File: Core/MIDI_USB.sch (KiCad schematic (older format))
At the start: 25 parts, among them J1 Conn_01x04, J4 Conn_01x06, SW1 SW_Push_DPDT, U1 ATSAMD21G15B-A, U10 TLE9250V, U9 MCP2517FD-xSL, Y1 20MHz

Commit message: Update MIDI_USB.sch
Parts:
- C35: value 22nF -> 4.7nF
- R4, R5: value 120 -> 56
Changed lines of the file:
@@
 P 10700 3850
 F 0 "C35" H 10815 3896 50  0000 L CNN
-F 1 "22nF" H 10815 3805 50  0000 L CNN
+F 1 "4.7nF" H 10815 3805 50  0000 L CNN
 F 2 "Capacitor_SMD:C_0603_1608Metric" H 10738 3700 50  0001 C CNN
 F 3 "~" H 10700 3850 50  0001 C CNN
@@
 P 10450 3200
 F 0 "R4" V 10243 3200 50  0000 C CNN
-F 1 "120" V 10334 3200 50  0000 C CNN
+F 1 "56" V 10334 3200 50  0000 C CNN
 F 2 "Resistor_SMD:R_0603_1608Metric" V 10380 3200 50  0001 C CNN
 F 3 "~" H 10450 3200 50  0001 C CNN
@@
 P 10450 3600
 F 0 "R5" V 10243 3600 50  0000 C CNN
-F 1 "120" V 10334 3600 50  0000 C CNN
+F 1 "56" V 10334 3600 50  0000 C CNN
 F 2 "Resistor_SMD:R_0603_1608Metric" V 10380 3600 50  0001 C CNN
 F 3 "~" H 10450 3600 50  0001 C CNN

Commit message: Add custom footprints
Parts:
- J1: footprint CustomLib:MicroMatch_04_Angled -> Custom_FP:MicroMatch_04_Angled
- SW1: footprint CustomLib:SlideDPDT_JS202011 -> Custom_FP:SlideDPDT_JS202011
- Y1: footprint CustomLib:Crystal_2pin_2.0x2.5mm -> Custom_FP:Crystal_2pin_2.0x2.5mm
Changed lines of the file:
@@
 F 0 "SW1" H 10000 3985 50  0000 C CNN
 F 1 "SW_Push_DPDT" H 10000 3894 50  0000 C CNN
-F 2 "CustomLib:SlideDPDT_JS202011" H 10000 3700 50  0001 C CNN
+F 2 "Custom_FP:SlideDPDT_JS202011" H 10000 3700 50  0001 C CNN
 F 3 "~" H 10000 3700 50  0001 C CNN
 	1    10000 3500
@@
 F 0 "J1" H 10680 5092 50  0000 L CNN
 F 1 "Conn_01x04" H 10680 5001 50  0000 L CNN
-F 2 "CustomLib:MicroMatch_04_Angled" H 10600 5100 50  0001 C CNN
+F 2 "Custom_FP:MicroMatch_04_Angled" H 10600 5100 50  0001 C CNN
 F 3 "~" H 10600 5100 50  0001 C CNN
 	1    10600 5100
@@
 F 0 "Y1" V 5704 4931 50  0000 L CNN
 F 1 "20MHz" V 5795 4931 50  0000 L CNN
-F 2 "CustomLib:Crystal_2pin_2.0x2.5mm" H 5750 4800 50  0001 C CNN
+F 2 "Custom_FP:Crystal_2pin_2.0x2.5mm" H 5750 4800 50  0001 C CNN
 F 3 "~" H 5750 4800 50  0001 C CNN
 	1    5750 4800

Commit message: Fix part number
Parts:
- U1: value ATSAMD21G15B-A -> ATSAMD21G17D-A; symbol MCU_Microchip_SAMD:ATSAMD21G15B-A -> MCU_Microchip_SAMD:ATSAMD21G17D-A
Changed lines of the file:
@@
 $EndDescr
 $Comp
-L MCU_Microchip_SAMD:ATSAMD21G15B-A U1
+L MCU_Microchip_SAMD:ATSAMD21G17D-A U1
 U 1 1 6095945E
 P 3000 3200
 F 0 "U1" H 3000 1211 50  0000 C CNN
-F 1 "ATSAMD21G15B-A" H 3000 1120 50  0000 C CNN
+F 1 "ATSAMD21G17D-A" H 3000 1120 50  0000 C CNN
 F 2 "Package_QFP:TQFP-48_7x7mm_P0.5mm" H 3900 1350 50  0001 C CNN
 F 3 "http://ww1.microchip.com/downloads/en/DeviceDoc/SAM_D21_DA1_Family_Data%20Sheet_DS40001882E.pdf" H 3000 4200 50  0001 C CNN

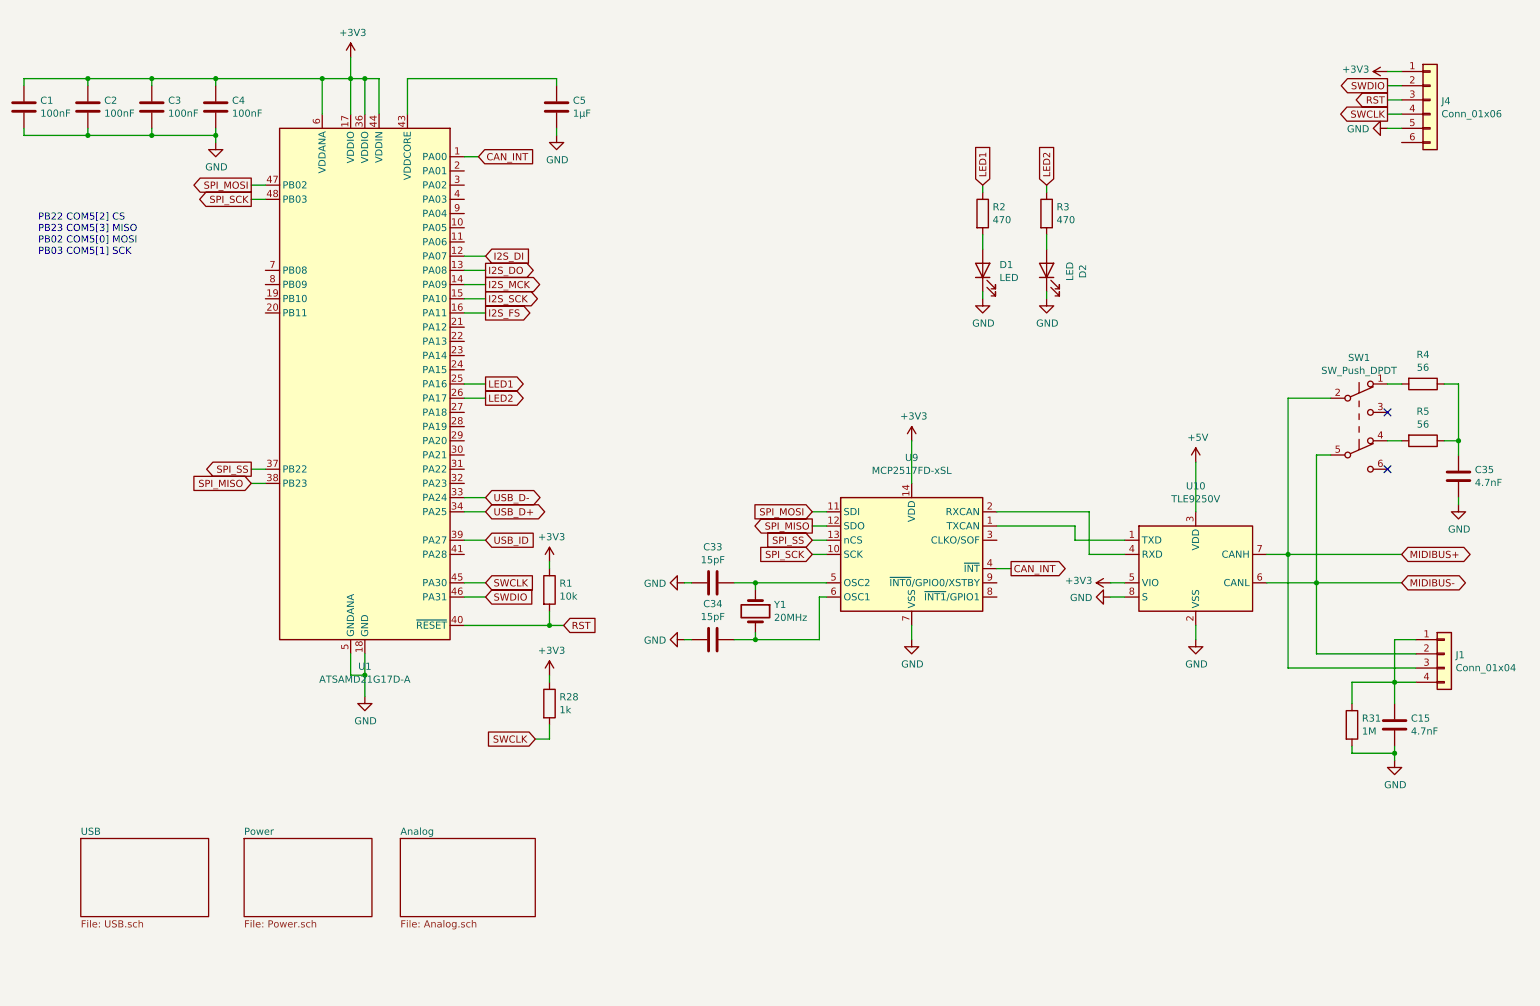
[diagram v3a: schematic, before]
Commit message: Add external EEPROM and RAM
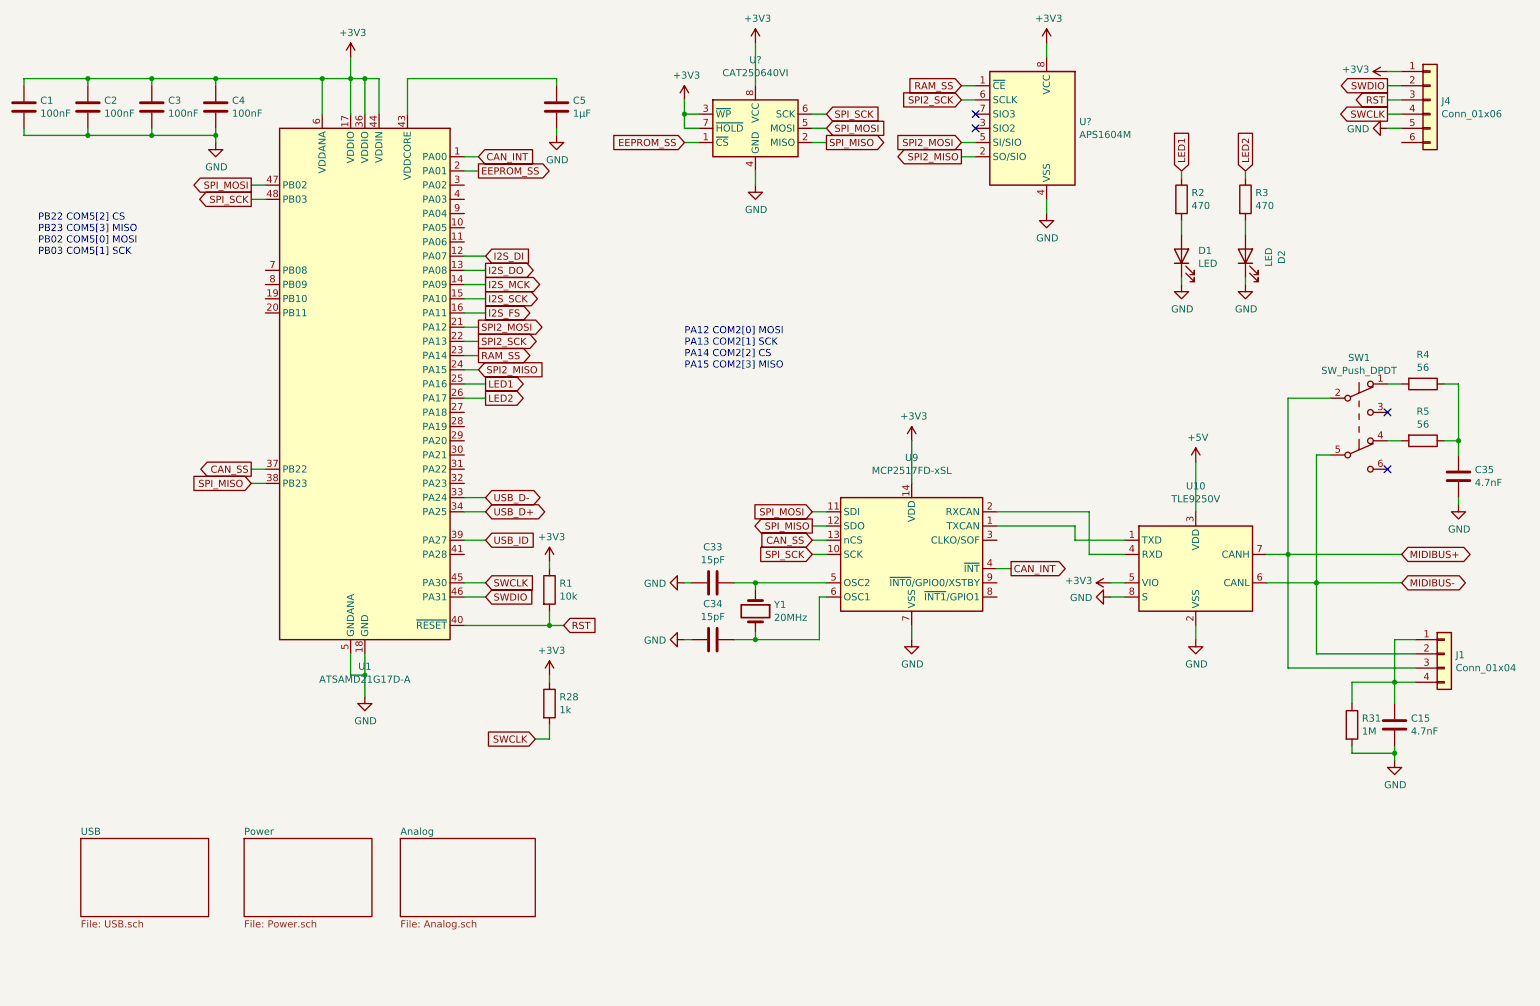
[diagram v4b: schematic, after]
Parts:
- added U?: CAT250640VI, Package_SO:SOIC-8_3.9x4.9mm_P1.27mm, symbol Memory_EEPROM:CAT250xxx
- added U?: APS1604M, Package_SO:SOIC-8_3.9x4.9mm_P1.27mm, symbol Memory_RAM:ESP-PSRAM32
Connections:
- net +3V3: now also U?.3 (~WP), U?.7 (~HOLD), U?.8 (VCC), U?.8 (VCC)
- net GND: now also U?.4 (GND), U?.4 (VSS)
- net SPI_MISO: now also U?.2 (MISO)
- net SPI_MOSI: now also U?.5 (MOSI)
- net SPI_SCK: now also U?.6 (SCK)
- net EEPROM_SS: now reaches U1.2 (PA01)
- net EEPROM_SS: now also U?.1 (~CS)
- net SPI2_MOSI: now reaches U1.21 (PA12)
- net SPI2_MOSI: now also U?.5 (SI/SIO)
- net SPI2_SCK: now reaches U1.22 (PA13)
- net SPI2_SCK: now also U?.6 (SCLK)
- net RAM_SS: now reaches U1.23 (PA14)
- net RAM_SS: now also U?.1 (~CE)
- net SPI2_MISO: now reaches U1.24 (PA15)
- net SPI2_MISO: now also U?.2 (SO/SIO)
- net SPI_SS renamed CAN_SS
- no-connect marks 2 -> 4
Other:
- note added: "PA12 COM2[0] MOSI\nPA13 COM2[1] SCK\nPA14 COM2[2] CS\nPA15 COM2[3] MISO"
- moved on the sheet: D1, D2, R2, R3
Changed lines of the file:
@@
 L Device:LED D2
 U 1 1 60984B3C
-P 7800 2400
-F 0 "D2" H 7793 2145 50  0000 C CNN
-F 1 "LED" H 7793 2236 50  0000 C CNN
-F 2 "LED_THT:LED_D3.0mm_Horizontal_O3.81mm_Z2.0mm" H 7800 2400 50  0001 C CNN
-F 3 "~" H 7800 2400 50  0001 C CNN
-	1    7800 2400
+P 9200 2300
+F 0 "D2" H 9193 2045 50  0000 C CNN
+F 1 "LED" H 9193 2136 50  0000 C CNN
+F 2 "LED_THT:LED_D3.0mm_Horizontal_O3.81mm_Z2.0mm" H 9200 2300 50  0001 C CNN
+F 3 "~" H 9200 2300 50  0001 C CNN
+	1    9200 2300
 	0    -1   -1   0
 $EndComp
@@
 L Device:LED D1
 U 1 1 60985304
-P 7350 2400
-F 0 "D1" V 7389 2282 50  0000 R CNN
-F 1 "LED" V 7298 2282 50  0000 R CNN
-F 2 "LED_THT:LED_D3.0mm_Horizontal_O1.27mm_Z2.0mm" H 7350 2400 50  0001 C CNN
-F 3 "~" H 7350 2400 50  0001 C CNN
-	1    7350 2400
+P 8750 2300
+F 0 "D1" V 8789 2182 50  0000 R CNN
+F 1 "LED" V 8698 2182 50  0000 R CNN
+F 2 "LED_THT:LED_D3.0mm_Horizontal_O1.27mm_Z2.0mm" H 8750 2300 50  0001 C CNN
+F 3 "~" H 8750 2300 50  0001 C CNN
+	1    8750 2300
 	0    -1   -1   0
 $EndComp
@@
 L Device:R R3
 U 1 1 60988515
-P 7800 2000
-F 0 "R3" H 7870 2046 50  0000 L CNN
-F 1 "470" H 7870 1955 50  0000 L CNN
-F 2 "Resistor_SMD:R_0603_1608Metric" V 7730 2000 50  0001 C CNN
-F 3 "~" H 7800 2000 50  0001 C CNN
-	1    7800 2000
+P 9200 1900
+F 0 "R3" H 9270 1946 50  0000 L CNN
+F 1 "470" H 9270 1855 50  0000 L CNN
+F 2 "Resistor_SMD:R_0603_1608Metric" V 9130 1900 50  0001 C CNN
+F 3 "~" H 9200 1900 50  0001 C CNN
+	1    9200 1900
 	1    0    0    -1
 $EndComp
@@
 L Device:R R2
 U 1 1 60988C27
-P 7350 2000
-F 0 "R2" H 7420 2046 50  0000 L CNN
-F 1 "470" H 7420 1955 50  0000 L CNN
-F 2 "Resistor_SMD:R_0603_1608Metric" V 7280 2000 50  0001 C CNN
-F 3 "~" H 7350 2000 50  0001 C CNN
-	1    7350 2000
+P 8750 1900
+F 0 "R2" H 8820 1946 50  0000 L CNN
+F 1 "470" H 8820 1855 50  0000 L CNN
+F 2 "Resistor_SMD:R_0603_1608Metric" V 8680 1900 50  0001 C CNN
+F 3 "~" H 8750 1900 50  0001 C CNN
+	1    8750 1900
 	1    0    0    -1
 $EndComp
@@
 L power:GND #PWR0111
 U 1 1 60988DE1
-P 7800 2600
-F 0 "#PWR0111" H 7800 2350 50  0001 C CNN
-F 1 "GND" H 7805 2427 50  0000 C CNN
-F 2 "" H 7800 2600 50  0001 C CNN
-F 3 "" H 7800 2600 50  0001 C CNN
-	1    7800 2600
+P 9200 2500
+F 0 "#PWR0111" H 9200 2250 50  0001 C CNN
+F 1 "GND" H 9205 2327 50  0000 C CNN
+F 2 "" H 9200 2500 50  0001 C CNN
+F 3 "" H 9200 2500 50  0001 C CNN
+	1    9200 2500
 	1    0    0    -1
 $EndComp
@@
 L power:GND #PWR0112
 U 1 1 60989143
-P 7350 2600
-F 0 "#PWR0112" H 7350 2350 50  0001 C CNN
-F 1 "GND" H 7355 2427 50  0000 C CNN
-F 2 "" H 7350 2600 50  0001 C CNN
-F 3 "" H 7350 2600 50  0001 C CNN
-	1    7350 2600
-	1    0    0    -1
-$EndComp
-Wire Wire Line
-	7350 2600 7350 2550
-Wire Wire Line
-	7800 2550 7800 2600
-Wire Wire Line
-	7800 2250 7800 2150
-Wire Wire Line
-	7350 2250 7350 2150
-Text GLabel 7350 1800 1    50   Input ~ 0
+P 8750 2500
+F 0 "#PWR0112" H 8750 2250 50  0001 C CNN
+F 1 "GND" H 8755 2327 50  0000 C CNN
+F 2 "" H 8750 2500 50  0001 C CNN
+F 3 "" H 8750 2500 50  0001 C CNN
+	1    8750 2500
+	1    0    0    -1
+$EndComp
+Wire Wire Line
+	8750 2500 8750 2450
+Wire Wire Line
+	9200 2450 9200 2500
+Wire Wire Line
+	9200 2150 9200 2050
+Wire Wire Line
+	8750 2150 8750 2050
+Text GLabel 8750 1700 1    50   Input ~ 0
 LED1
-Text GLabel 7800 1800 1    50   Input ~ 0
+Text GLabel 9200 1700 1    50   Input ~ 0
 LED2
 Wire Wire Line
-	7800 1800 7800 1850
-Wire Wire Line
-	7350 1850 7350 1800
+	9200 1700 9200 1750
+Wire Wire Line
+	8750 1750 8750 1700
 Text GLabel 3850 4300 2    50   Input ~ 0
 USB_ID
@@
 SPI_MOSI
 Text GLabel 6150 4300 0    50   Input ~ 0
-SPI_SS
+CAN_SS
 Text GLabel 6150 4400 0    50   Input ~ 0
 SPI_SCK
@@
 PB22 COM5[2] CS\nPB23 COM5[3] MISO\nPB02 COM5[0] MOSI\nPB03 COM5[1] SCK
 Text GLabel 2200 3800 0    50   Output ~ 0
-SPI_SS
+CAN_SS
 Text GLabel 2200 3900 0    50   Input ~ 0
 SPI_MISO
@@
 Text GLabel 4200 5700 0    50   Input ~ 0
 SWCLK
+$Comp
+L Memory_EEPROM:CAT250xxx U?
+U 1 1 62CF50E4
+P 5750 1400
+F 0 "U?" H 5750 1881 50  0000 C CNN
+F 1 "CAT250640VI" H 5750 1790 50  0000 C CNN
+F 2 "Package_SO:SOIC-8_3.9x4.9mm_P1.27mm" H 5750 1400 50  0001 C CNN
+F 3 "http://www.onsemi.com/PowerSolutions/product.do?id=CAT25040" H 5750 1400 50  0001 C CNN
+	1    5750 1400
+	1    0    0    -1
+$EndComp
+$Comp
+L Memory_RAM:ESP-PSRAM32 U?
+U 1 1 62CFA564
+P 7700 1400
+F 0 "U?" H 7370 1446 50  0000 R CNN
+F 1 "APS1604M" H 7370 1355 50  0000 R CNN
+F 2 "Package_SO:SOIC-8_3.9x4.9mm_P1.27mm" H 7700 800 50  0001 C CNN
+F 3 "https://www.espressif.com/sites/default/files/documentation/esp-psram32_datasheet_en.pdf" H 7300 1900 50  0001 C CNN
+	1    7700 1400
+	-1   0    0    -1
+$EndComp
+$Comp
+L power:+3V3 #PWR?
+U 1 1 62D0BAED
+P 7800 800
+F 0 "#PWR?" H 7800 650 50  0001 C CNN
+F 1 "+3V3" H 7815 973 50  0000 C CNN
+F 2 "" H 7800 800 50  0001 C CNN
+F 3 "" H 7800 800 50  0001 C CNN
+	1    7800 800
+	1    0    0    -1
+$EndComp
+$Comp
+L power:+3V3 #PWR?
+U 1 1 62D0BCD9
+P 5750 800
+F 0 "#PWR?" H 5750 650 50  0001 C CNN
+F 1 "+3V3" H 5765 973 50  0000 C CNN
+F 2 "" H 5750 800 50  0001 C CNN
+F 3 "" H 5750 800 50  0001 C CNN
+	1    5750 800
+	1    0    0    -1
+$EndComp
+Wire Wire Line
+	5750 800  5750 1100
+Wire Wire Line
+	7800 800  7800 900
+Wire Wire Line
+	7800 2000 7800 1900
+Wire Wire Line
+	5750 1800 5750 1700
+$Comp
+L power:GND #PWR?
+U 1 1 62D21FFD
+P 5750 1800
+F 0 "#PWR?" H 5750 1550 50  0001 C CNN
+F 1 "GND" H 5755 1627 50  0000 C CNN
+F 2 "" H 5750 1800 50  0001 C CNN
+F 3 "" H 5750 1800 50  0001 C CNN
+	1    5750 1800
+	1    0    0    -1
+$EndComp
+$Comp
+L power:GND #PWR?
+U 1 1 62D228FF
+P 7800 2000
+F 0 "#PWR?" H 7800 1750 50  0001 C CNN
+F 1 "GND" H 7805 1827 50  0000 C CNN
+F 2 "" H 7800 2000 50  0001 C CNN
+F 3 "" H 7800 2000 50  0001 C CNN
+	1    7800 2000
+	1    0    0    -1
+$EndComp
+NoConn ~ 7300 1400
+NoConn ~ 7300 1300
+Text GLabel 3800 1700 2    50   Output ~ 0
+EEPROM_SS
+Text GLabel 5250 1500 0    50   Input ~ 0
+EEPROM_SS
+Text GLabel 7200 1200 0    50   Input ~ 0
+SPI2_SCK
+Text GLabel 7200 1500 0    50   Input ~ 0
+SPI2_MOSI
+Text GLabel 7200 1600 0    50   Output ~ 0
+SPI2_MISO
+Wire Wire Line
+	7200 1600 7300 1600
+Wire Wire Line
+	7300 1500 7200 1500
+Wire Wire Line
+	7200 1200 7300 1200
+Wire Wire Line
+	5350 1500 5250 1500
+Text GLabel 6250 1300 2    50   Input ~ 0
+SPI_SCK
+Text GLabel 6250 1400 2    50   Input ~ 0
+SPI_MOSI
+Text GLabel 6250 1500 2    50   Output ~ 0
+SPI_MISO
+Wire Wire Line
+	6250 1500 6150 1500
+Wire Wire Line
+	6150 1400 6250 1400
+Wire Wire Line
+	6250 1300 6150 1300
+Text GLabel 7200 1100 0    50   Input ~ 0
+RAM_SS
+Wire Wire Line
+	7200 1100 7300 1100
+$Comp
+L power:+3V3 #PWR?
+U 1 1 62D75718
+P 5250 1200
+F 0 "#PWR?" H 5250 1050 50  0001 C CNN
+F 1 "+3V3" H 5265 1373 50  0000 C CNN
+F 2 "" H 5250 1200 50  0001 C CNN
+F 3 "" H 5250 1200 50  0001 C CNN
+	1    5250 1200
+	1    0    0    -1
+$EndComp
+Wire Wire Line
+	5250 1300 5350 1300
+Wire Wire Line
+	5350 1400 5250 1400
+Wire Wire Line
+	5250 1200 5250 1300
+Connection ~ 5250 1300
+Wire Wire Line
+	5250 1300 5250 1400
+Wire Wire Line
+	3800 1700 3700 1700
+Text GLabel 3800 2900 2    50   Output ~ 0
+SPI2_SCK
+Text GLabel 3800 2800 2    50   Output ~ 0
+SPI2_MOSI
+Text GLabel 3800 3100 2    50   Input ~ 0
+SPI2_MISO
+Wire Wire Line
+	3800 3100 3700 3100
+Wire Wire Line
+	3700 2800 3800 2800
+Wire Wire Line
+	3800 2900 3700 2900
+Text GLabel 3800 3000 2    50   Output ~ 0
+RAM_SS
+Wire Wire Line
+	3800 3000 3700 3000
+Text Notes 5250 3100 0    50   ~ 0
+PA12 COM2[0] MOSI\nPA13 COM2[1] SCK\nPA14 COM2[2] CS\nPA15 COM2[3] MISO
 $EndSCHEMATC
